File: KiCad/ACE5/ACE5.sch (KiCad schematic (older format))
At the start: 25 parts, among them X2 32MHz

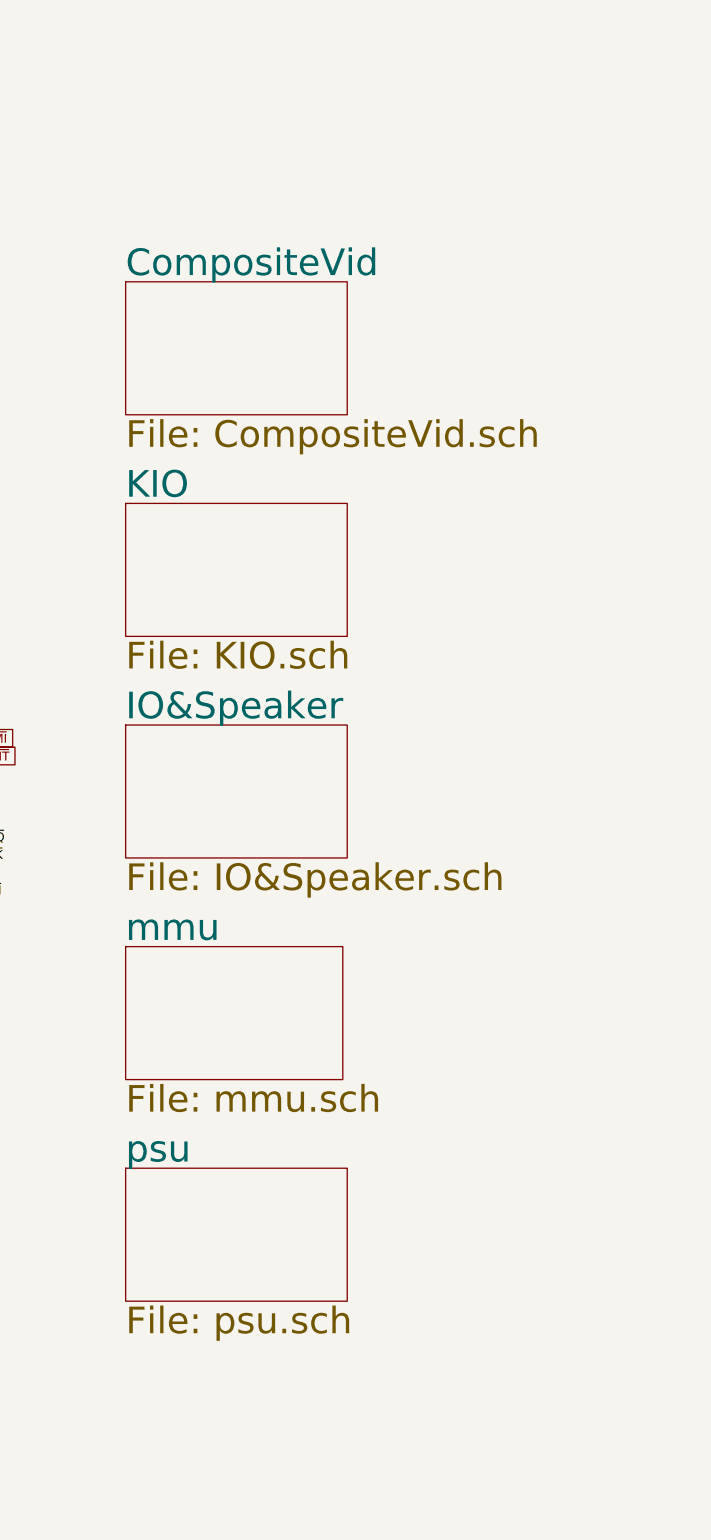
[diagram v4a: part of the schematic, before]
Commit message: Address inconsistencies between 3,4,5. Renumber part to reflect version. Relocate Z80 parts library to separate repository.
https://github.com/flypie/Z80-CPU-for-KiCAD

Signed-off-by: John Bradley <flypie@rocketmail.com>
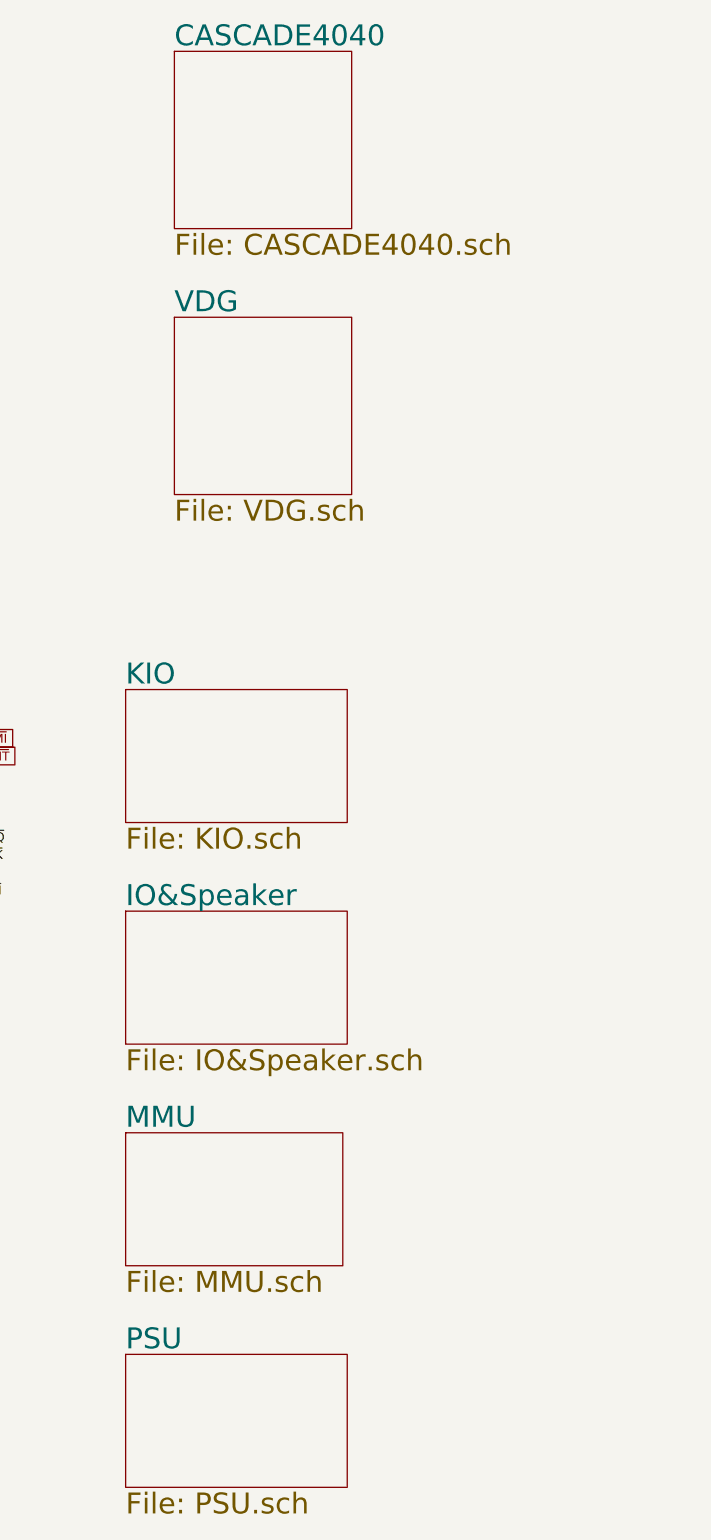
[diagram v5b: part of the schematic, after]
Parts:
- Z100, Z29: footprint Package_DIP:DIP-16_W7.62mm -> Package_DIP:DIP-16_W7.62mm_Socket
- Z102, Z19, Z22, Z23, Z25: footprint Package_DIP:DIP-14_W7.62mm -> Package_DIP:DIP-14_W7.62mm_Socket
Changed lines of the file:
@@
 EESchema Schematic File Version 4
-LIBS:ACE5-cache
 EELAYER 30 0
 EELAYER END
 $Descr A4 11693 8268
 encoding utf-8
-Sheet 1 6
+Sheet 1 7
 Title "ACE5"
 Date "2019-09-15"
@@
 NoConn ~ 5425 6550
 $Sheet
-S 11725 2550 1250 750
+S 11725 3600 1250 750
 U 5DD74AB7
-F0 "KIO" 150
-F1 "KIO.sch" 150
+F0 "KIO" 118
+F1 "KIO.sch" 118
 $EndSheet
 $Sheet
-S 11725 1300 1250 750
+S 12000 1500 1000 1000
 U 5DAF6158
-F0 "CompositeVid" 150
-F1 "CompositeVid.sch" 150
+F0 "VDG" 118
+F1 "VDG.sch" 118
 $EndSheet
 Text GLabel 1700 1100 2    50   Input ~ 0
@@
 F 0 "Z29" H 2825 2800 50  0000 C CNN
 F 1 "74AHCT138" H 2825 2700 50  0000 C CNN
-F 2 "Package_DIP:DIP-16_W7.62mm" H 2825 1975 50  0001 C CNN
+F 2 "Package_DIP:DIP-16_W7.62mm_Socket" H 2825 1975 50  0001 C CNN
 F 3 "http:~/www.ti.com/lit/gpn/sn74LS138" H 2825 1975 50  0001 C CNN
 	1    2825 1975
@@
 F 0 "Z19" H -1500 2450 50  0000 C CNN
 F 1 "74AHCT00" H -1500 2350 50  0000 C CNN
-F 2 "Package_DIP:DIP-14_W7.62mm" H -1500 2100 50  0001 C CNN
+F 2 "Package_DIP:DIP-14_W7.62mm_Socket" H -1500 2100 50  0001 C CNN
 F 3 "http:~/www.ti.com/lit/gpn/sn74ls00" H -1500 2100 50  0001 C CNN
 	3    -1500 2100
@@
 F 0 "Z19" H -640 2470 50  0000 C CNN
 F 1 "74AHCT00" H -640 2370 50  0000 C CNN
-F 2 "Package_DIP:DIP-14_W7.62mm" H -675 2100 50  0001 C CNN
+F 2 "Package_DIP:DIP-14_W7.62mm_Socket" H -675 2100 50  0001 C CNN
 F 3 "http:~/www.ti.com/lit/gpn/sn74ls00" H -675 2100 50  0001 C CNN
 	4    -675 2100
@@
 F 0 "Z102" V 3325 3200 50  0000 L CNN
 F 1 "SN74AHCT04N" V 3375 3200 50  0000 L CNN
-F 2 "Package_DIP:DIP-14_W7.62mm" H 3375 3000 50  0001 C CNN
+F 2 "Package_DIP:DIP-14_W7.62mm_Socket" H 3375 3000 50  0001 C CNN
 F 3 "http:~/www.ti.com/lit/gpn/sn74LS04" H 3375 3000 50  0001 C CNN
 	6    3375 3000
@@
 F 0 "Z100" H 5000 7075 50  0000 C CNN
 F 1 "74AHCT139" H 5000 6975 50  0000 C CNN
-F 2 "Package_DIP:DIP-16_W7.62mm" H 4925 6650 50  0001 C CNN
+F 2 "Package_DIP:DIP-16_W7.62mm_Socket" H 4925 6650 50  0001 C CNN
 F 3 "http://www.ti.com/lit/gpn/sn74LS139" H 4925 6650 50  0001 C CNN
 	2    4925 6650
@@
 F 0 "Z23" H -2300 1450 50  0000 C CNN
 F 1 "74AHCT86" H -2300 1350 50  0000 C CNN
-F 2 "Package_DIP:DIP-14_W7.62mm" H -2300 1100 50  0001 C CNN
+F 2 "Package_DIP:DIP-14_W7.62mm_Socket" H -2300 1100 50  0001 C CNN
 F 3 "74xx~74ls86.pdf" H -2300 1100 50  0001 C CNN
 	1    -2300 1100
@@
 F 0 "Z23" H -1550 1450 50  0000 C CNN
 F 1 "74AHCT86" H -1550 1350 50  0000 C CNN
-F 2 "Package_DIP:DIP-14_W7.62mm" H -1550 1100 50  0001 C CNN
+F 2 "Package_DIP:DIP-14_W7.62mm_Socket" H -1550 1100 50  0001 C CNN
 F 3 "74xx~74ls86.pdf" H -1550 1100 50  0001 C CNN
 	2    -1550 1100
@@
 F 0 "Z102" H 3370 6890 50  0000 C CNN
 F 1 "SN74AHCT04N" H 3370 6790 50  0000 C CNN
-F 2 "Package_DIP:DIP-14_W7.62mm" H 3325 6550 50  0001 C CNN
+F 2 "Package_DIP:DIP-14_W7.62mm_Socket" H 3325 6550 50  0001 C CNN
 F 3 "http:~/www.ti.com/lit/gpn/sn74LS04" H 3325 6550 50  0001 C CNN
 	2    3325 6550
@@
 F 0 "Z25" H -2280 2460 50  0000 C CNN
 F 1 "74AHCT02" H -2280 2360 50  0000 C CNN
-F 2 "Package_DIP:DIP-14_W7.62mm" H -2325 2100 50  0001 C CNN
+F 2 "Package_DIP:DIP-14_W7.62mm_Socket" H -2325 2100 50  0001 C CNN
 F 3 "http:~/www.ti.com/lit/gpn/sn74ls02" H -2325 2100 50  0001 C CNN
 	3    -2325 2100
@@
 Connection ~ 7775 2275
 $Sheet
-S 11725 3800 1250 750
+S 11725 4850 1250 750
 U 5DBBBE50
-F0 "IO&Speaker" 150
-F1 "IO&Speaker.sch" 150
+F0 "IO&Speaker" 118
+F1 "IO&Speaker.sch" 118
 $EndSheet
 Wire Wire Line
@@
 F 0 "Z102" H -2305 3040 50  0000 C CNN
 F 1 "SN74AHCT04N" H -2305 2940 50  0000 C CNN
-F 2 "Package_DIP:DIP-14_W7.62mm" H -2350 2700 50  0001 C CNN
+F 2 "Package_DIP:DIP-14_W7.62mm_Socket" H -2350 2700 50  0001 C CNN
 F 3 "http:~/www.ti.com/lit/gpn/sn74LS04" H -2350 2700 50  0001 C CNN
 	5    -2350 2700
@@
 F 0 "Z100" H 3825 1350 50  0000 C CNN
 F 1 "74AHCT139" H 3825 1250 50  0000 C CNN
-F 2 "Package_DIP:DIP-16_W7.62mm" H 3825 925 50  0001 C CNN
+F 2 "Package_DIP:DIP-16_W7.62mm_Socket" H 3825 925 50  0001 C CNN
 F 3 "http://www.ti.com/lit/gpn/sn74LS139" H 3825 925 50  0001 C CNN
 	1    3825 925
@@
 NoConn ~ -1800 2000
 $Sheet
-S 11725 5050 1225 750
+S 11725 6100 1225 750
 U 5DC61528
-F0 "mmu" 150
-F1 "mmu.sch" 150
-$EndSheet
-$Sheet
-S 11725 6300 1250 750
-U 5DE39253
-F0 "psu" 150
-F1 "psu.sch" 150
+F0 "MMU" 118
+F1 "MMU.sch" 118
 $EndSheet
 Text GLabel 6400 4250 0    50   Input ~ 0
@@
 F 0 "Z22" V 4300 4300 50  0000 R CNN
 F 1 "74AHCT11" V 4400 4300 50  0000 R CNN
-F 2 "Package_DIP:DIP-14_W7.62mm" H 4375 4525 50  0001 C CNN
+F 2 "Package_DIP:DIP-14_W7.62mm_Socket" H 4375 4525 50  0001 C CNN
 F 3 "http:~/www.ti.com/lit/gpn/sn74AHCT11" H 4375 4525 50  0001 C CNN
 	3    4375 4525
@@
 F 0 "Z102" H -1505 3040 50  0000 C CNN
 F 1 "SN74AHCT04N" H -1505 2940 50  0000 C CNN
-F 2 "Package_DIP:DIP-14_W7.62mm" H -1550 2700 50  0001 C CNN
+F 2 "Package_DIP:DIP-14_W7.62mm_Socket" H -1550 2700 50  0001 C CNN
 F 3 "http:~/www.ti.com/lit/gpn/sn74LS04" H -1550 2700 50  0001 C CNN
 	1    -1550 2700
@@
 NoConn ~ -1250 2700
 NoConn ~ -1850 2700
+$Sheet
+S 11725 7350 1250 750
+U 5DE39253
+F0 "PSU" 118
+F1 "PSU.sch" 118
+$EndSheet
+$Sheet
+S 12000 0    1000 1000
+U 6018B0CE
+F0 "CASCADE4040" 118
+F1 "CASCADE4040.sch" 118
+$EndSheet
 $EndSCHEMATC

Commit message: Rearrange boards 4 & 5. Make IC numbering consistent.
Signed-off-by: John Bradley <flypie@rocketmail.com>
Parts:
- removed unit 1 of Z100
- removed unit 1 of Z102
- removed unit 5 of Z102
- removed unit 6 of Z102
- removed Z104: 74AHCT30D, Package_SO:SOIC-14_3.9x8.7mm_P1.27mm, symbol 74xx:74LS30
- removed Z19: 74AHCT00, Package_DIP:DIP-14_W7.62mm_Socket, symbol 74xx:74HCT00
- removed Z29: 74AHCT138, Package_DIP:DIP-16_W7.62mm_Socket, symbol 74xx:74LS138
- added Z19: 74AHCT00, Package_DIP:DIP-14_W7.62mm_Socket, symbol 74xx:74LS00
- added unit 3 of Z23
- added Z404: 74LS21, Package_DIP:DIP-14_W7.62mm_Socket, symbol 74xx:74LS21
- Z306: renamed from Z102; value SN74AHCT04N -> 74AHCT04
- renumbered Z100 to Z307, Z101 to Z308
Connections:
- net A6: now also Z308.12
- net A7: no longer Z308.12
- net ~RAMSEL: now reaches R32.2, Z3-4.6 (~CE1)
- net ~ROMSEL: now reaches Z1-2.22 (CE), Z1-2.24 (OE)
- net ~ROMSEL: no longer Z22.8
- no-connect marks 27 -> 35
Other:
- moved on the sheet: C100, C101, C7, Logo1, Logo2, R25, R32, X2, Z0A, Z0B, Z1-2, Z23A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

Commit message: Remove SMD.
Standardise Z180 and add Z380.


Signed-off-by: John Bradley <flypie@rocketmail.com>
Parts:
- C100: value 22p -> 33pf; footprint Capacitor_THT:C_Disc_D4.3mm_W1.9mm_P5.00mm -> Capacitor_THT:C_Disc_D3.0mm_W1.6mm_P2.50mm
- C101: value 42p -> 33pf; footprint Capacitor_THT:C_Disc_D4.3mm_W1.9mm_P5.00mm -> Capacitor_THT:C_Disc_D3.0mm_W1.6mm_P2.50mm
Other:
- moved on the sheet: C100, C101, C7, R25, R32, X2, Z0A, Z0B, Z1-2, Z3-4, Z306B, Z307B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
